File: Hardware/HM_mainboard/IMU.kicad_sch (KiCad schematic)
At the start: 12 parts, among them U5 BNO055, U6 MC6470

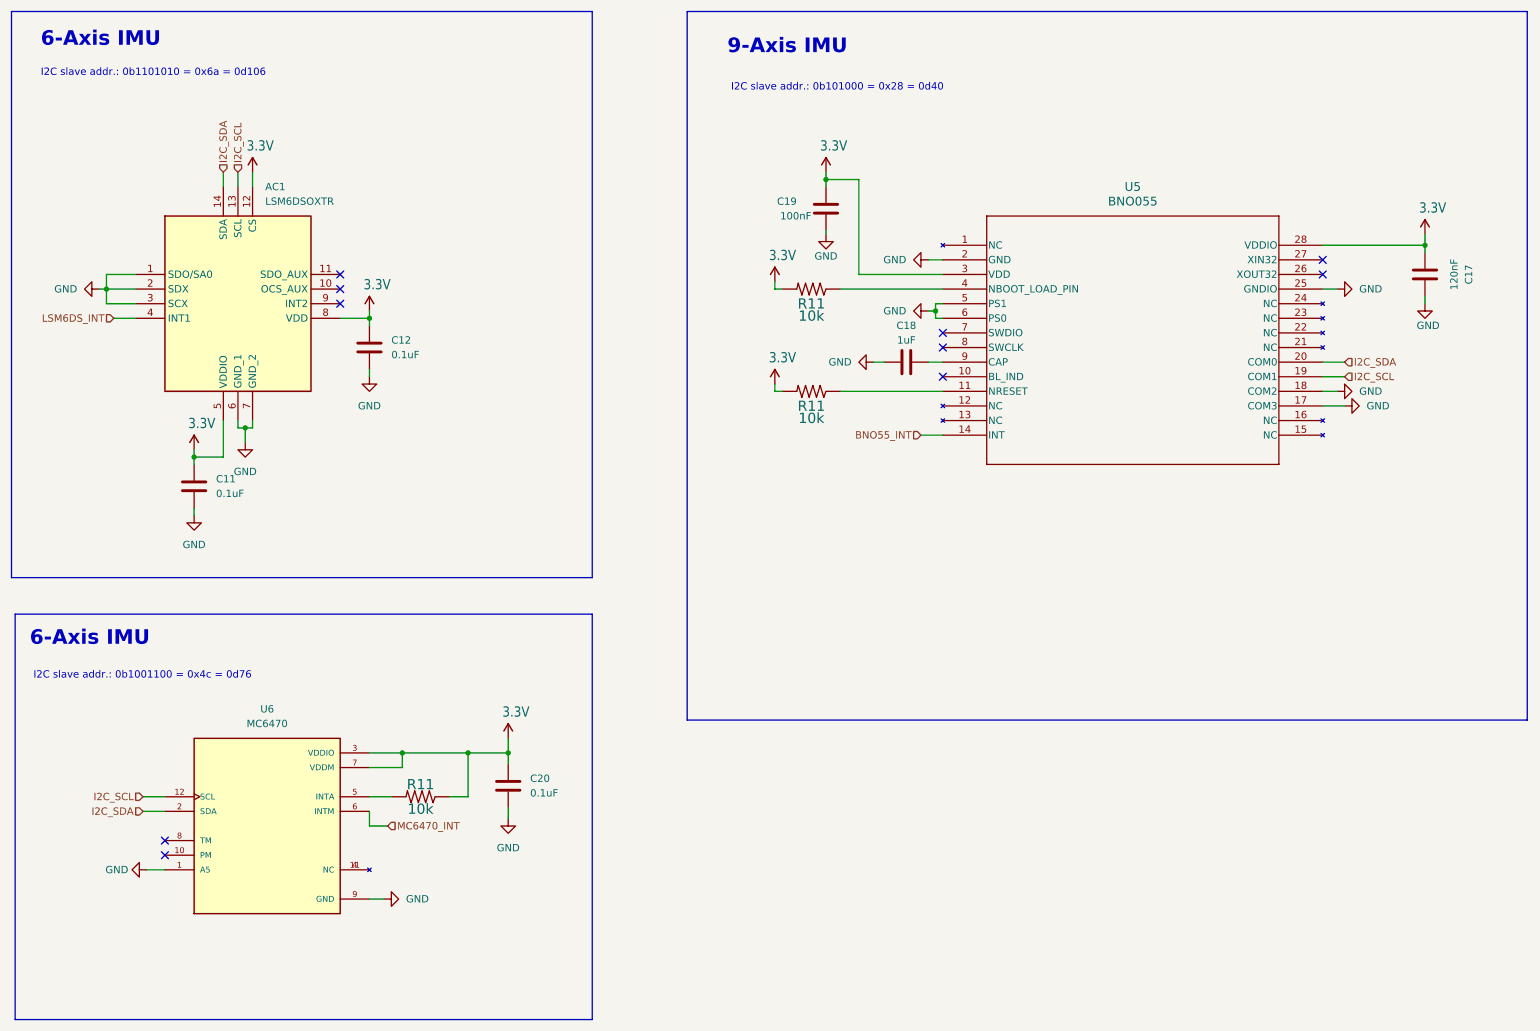
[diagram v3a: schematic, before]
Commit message: Added pull-ups to i2c connections
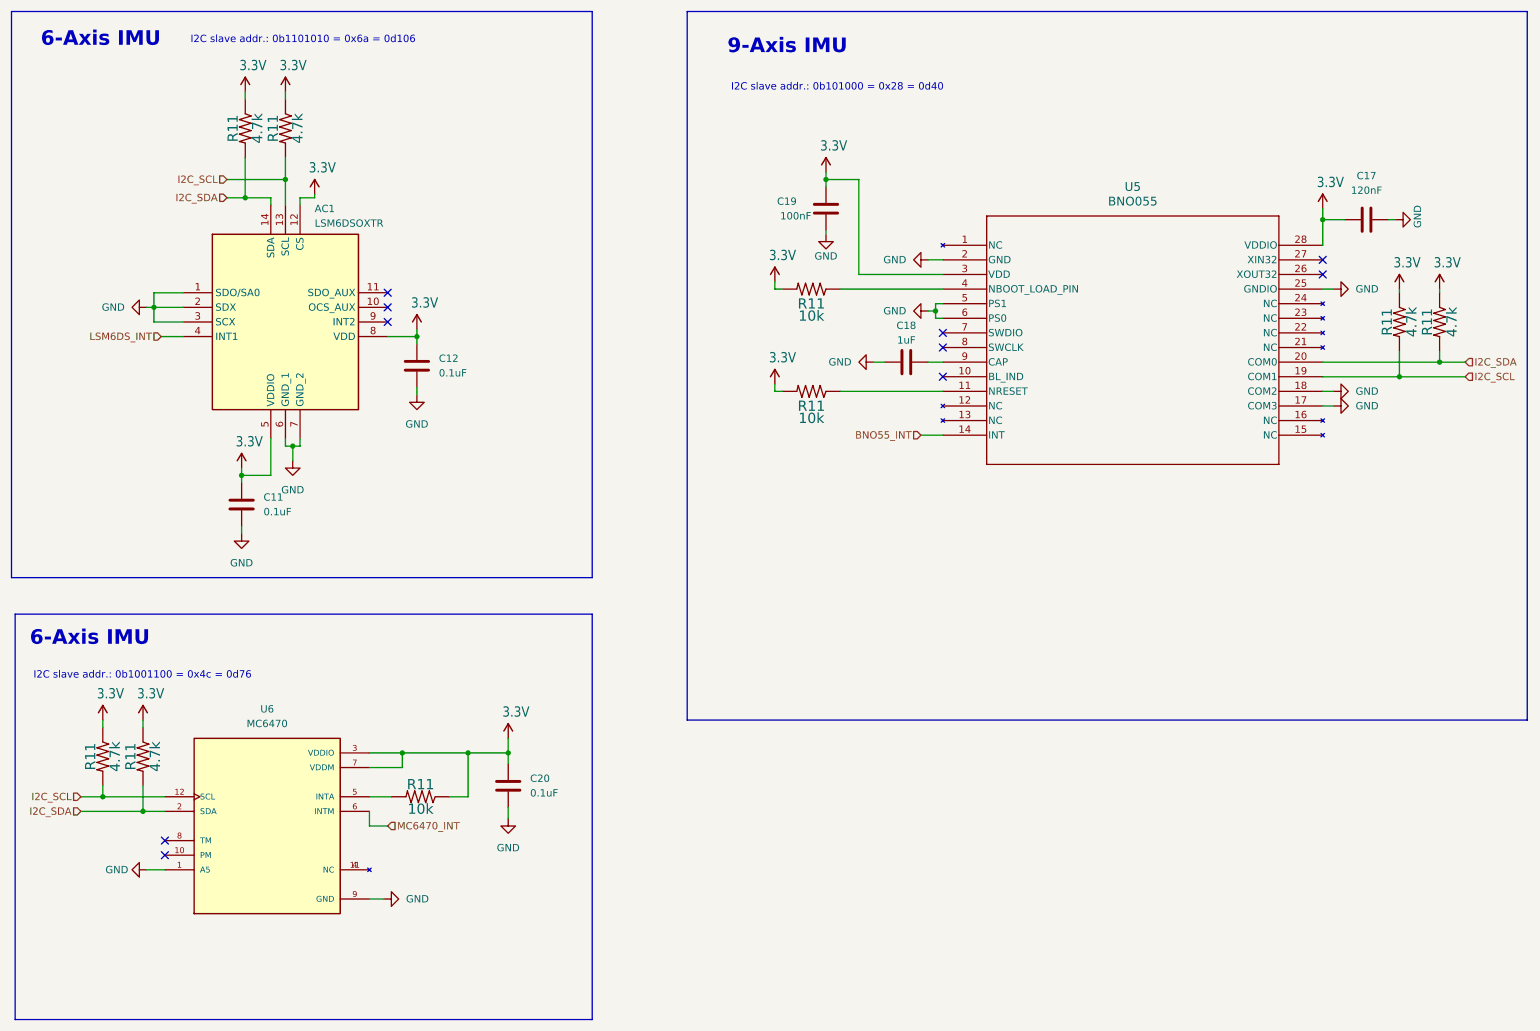
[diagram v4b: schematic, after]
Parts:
- added R11 (x6): 4.7k, Resistor_SMD:R_0603_1608Metric_Pad0.98x0.95mm_HandSolder, symbol esp32-thing-eagle-import:10KOHM-1/10W-1%(0603)0603
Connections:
- net 3.3V: now also R11.1, R11.1, R11.1, R11.1, R11.1, R11.1
- net I2C_SCL: now also R11.2, R11.2, R11.2
- net I2C_SDA: now also R11.2, R11.2, R11.2
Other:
- moved on the sheet: AC1, C11, C12, C17

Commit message: Started component placement for PCB
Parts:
- renumbered C11 to C15, C12 to C16, C20 to C17, C19 to C18, C18 to C19, C17 to C20, U6 to U5, U5 to U6

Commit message: Updated footprint of auxiliary jacks, routed first version of PCB
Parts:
- removed R11 (x6): 4.7k, Resistor_SMD:R_0603_1608Metric_Pad0.98x0.95mm_HandSolder, symbol esp32-thing-eagle-import:10KOHM-1/10W-1%(0603)0603

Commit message: Added BOM
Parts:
- AC1: Mouser (none) -> LSM6DSOXTR
- C15, C16, C17: value 0.1uF -> 100nF; Digikey (none) -> 1276-CL10B104KB8NNNLCT-ND; Mouser (none) -> 581-06035C104K4; RS Components (none) -> 200-6519
- C18: Digikey (none) -> 1276-CL10B104KB8NNNLCT-ND; Mouser (none) -> 581-06035C104K4; RS Components (none) -> 200-6519
- C19: value 1uF -> 1.0uF-25V-(+80/-20%); Mouser (none) -> F921E105KPA
- C20: value 120nF -> 100nF; Digikey (none) -> 1276-CL10B104KB8NNNLCT-ND; Mouser (none) -> 581-06035C104K4; RS Components (none) -> 200-6519
- U5: Mouser (none) -> MC6470; Mouser Price/Stock (none) -> https://www.mouser.at/ProductDetail/MEMSIC/MC6470?qs=u6%2FI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
- U6: Digikey (none) -> 828-1058; Mouser Price/Stock (none) -> https://www.digikey.at/en/products/detail/bosch-sensortec/B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
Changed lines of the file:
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@@
       (effects (font (size 1.27 1.27)))
     )
-    (property "Value" "1uF" (at 172.085 73.66 90)
+    (property "Value" "1.0uF-25V-(+80/-20%)" (at 172.085 73.66 90)
       (effects (font (size 1.27 1.27)))
     )
@@
     )
     (property "Datasheet" "~" (at 172.085 77.47 0)
+      (effects (font (size 1.27 1.27)) hide)
+    )
+    (property "Mouser" "F921E105KPA" (at 172.085 77.47 0)
+      (effects (font (size 1.27 1.27)) hide)
+    )
+    (property "Reichelt" "" (at 172.085 77.47 0)
       (effects (font (size 1.27 1.27)) hide)
     )
@@
       (effects (font (size 1.27 1.27)) hide)
     )
+    (property "Reichelt" "" (at 155.575 64.77 0)
+      (effects (font (size 1.27 1.27)) hide)
+    )
     (pin "1")
     (pin "2")
@@
       (effects (font (size 1.27 1.27)))
     )
-    (property "Value" "120nF" (at 252.095 47.625 90)
+    (property "Value" "100nF" (at 252.095 47.625 90)
       (effects (font (size 1.27 1.27)))
     )
@@
     )
     (property "Datasheet" "~" (at 252.095 52.705 0)
+      (effects (font (size 1.27 1.27)) hide)
+    )
+    (property "Reichelt" "" (at 252.095 52.705 0)
+      (effects (font (size 1.27 1.27)) hide)
+    )
+    (property "Digikey" "1276-CL10B104KB8NNNLCT-ND" (at 252.095 52.705 0)
+      (effects (font (size 1.27 1.27)) hide)
+    )
+    (property "Mouser" "581-06035C104K4" (at 252.095 52.705 0)
+      (effects (font (size 1.27 1.27)) hide)
+    )
+    (property "RS Components" "200-6519" (at 252.095 52.705 0)
       (effects (font (size 1.27 1.27)) hide)
     )
@@
       (effects (font (size 1.27 1.27)) (justify left))
     )
-    (property "Value" "0.1uF" (at 60.325 103.505 0)
+    (property "Value" "100nF" (at 60.325 103.505 0)
       (effects (font (size 1.27 1.27)) (justify left))
     )
@@
     )
     (property "Datasheet" "~" (at 56.515 102.235 0)
+      (effects (font (size 1.27 1.27)) hide)
+    )
+    (property "Reichelt" "" (at 56.515 102.235 0)
+      (effects (font (size 1.27 1.27)) hide)
+    )
+    (property "Digikey" "1276-CL10B104KB8NNNLCT-ND" (at 56.515 102.235 0)
+      (effects (font (size 1.27 1.27)) hide)
+    )
+    (property "Mouser" "581-06035C104K4" (at 56.515 102.235 0)
+      (effects (font (size 1.27 1.27)) hide)
+    )
+    (property "RS Components" "200-6519" (at 56.515 102.235 0)
       (effects (font (size 1.27 1.27)) hide)
     )
@@
       (effects (font (size 1.27 1.27)) (justify bottom) hide)
     )
-    (property "Datasheet" "" (at 60.96 158.115 0)
+    (property "Datasheet" "https://www.mouser.at/datasheet/2/821/MC6470_Datasheet_APS_048_0033v1_7_1-3003085.pdf" (at 60.96 158.115 0)
       (effects (font (size 1.27 1.27)) hide)
     )
     (property "MF" "Mcube Inc." (at 60.96 158.115 0)
       (effects (font (size 1.27 1.27)) (justify bottom) hide)
+    )
+    (property "Mouser" "MC6470" (at 60.96 158.115 0)
+      (effects (font (size 1.27 1.27)) hide)
+    )
+    (property "Mouser Price/Stock" "https://www.mouser.at/ProductDetail/MEMSIC/MC6470?qs=u6%2FIMcj1sDuOjN54xX4NKQ%3D%3D" (at 60.96 158.115 0)
+      (effects (font (size 1.27 1.27)) hide)
+    )
+    (property "Reichelt" "" (at 60.96 158.115 0)
+      (effects (font (size 1.27 1.27)) hide)
     )
     (pin "1")
@@
       (effects (font (size 1.27 1.27)) (justify left))
     )
-    (property "Value" "0.1uF" (at 90.805 79.375 0)
+    (property "Value" "100nF" (at 90.805 79.375 0)
       (effects (font (size 1.27 1.27)) (justify left))
     )
@@
     )
     (property "Datasheet" "~" (at 86.995 78.105 0)
+      (effects (font (size 1.27 1.27)) hide)
+    )
+    (property "Reichelt" "" (at 86.995 78.105 0)
+      (effects (font (size 1.27 1.27)) hide)
+    )
+    (property "Digikey" "1276-CL10B104KB8NNNLCT-ND" (at 86.995 78.105 0)
+      (effects (font (size 1.27 1.27)) hide)
+    )
+    (property "Mouser" "581-06035C104K4" (at 86.995 78.105 0)
+      (effects (font (size 1.27 1.27)) hide)
+    )
+    (property "RS Components" "200-6519" (at 86.995 78.105 0)
       (effects (font (size 1.27 1.27)) hide)
     )
@@
       (effects (font (size 1.27 1.27)) (justify left))
     )
-    (property "Value" "0.1uF" (at 106.68 152.4 0)
+    (property "Value" "100nF" (at 106.68 152.4 0)
       (effects (font (size 1.27 1.27)) (justify left))
     )
@@
     )
     (property "Datasheet" "~" (at 102.87 151.13 0)
+      (effects (font (size 1.27 1.27)) hide)
+    )
+    (property "Reichelt" "" (at 102.87 151.13 0)
+      (effects (font (size 1.27 1.27)) hide)
+    )
+    (property "Digikey" "1276-CL10B104KB8NNNLCT-ND" (at 102.87 151.13 0)
+      (effects (font (size 1.27 1.27)) hide)
+    )
+    (property "Mouser" "581-06035C104K4" (at 102.87 151.13 0)
+      (effects (font (size 1.27 1.27)) hide)
+    )
+    (property "RS Components" "200-6519" (at 102.87 151.13 0)
       (effects (font (size 1.27 1.27)) hide)
     )
@@
     (property "Datasheet" "https://www.bosch-sensortec.com/media/boschsensortec/downloads/datasheets/bst-bno055-ds000.pdf" (at 178.435 57.15 0)
       (effects (font (size 1.27 1.27) italic) hide)
+    )
+    (property "Digikey" "828-1058" (at 178.435 57.15 0)
+      (effects (font (size 1.27 1.27)) hide)
+    )
+    (property "Mouser Price/Stock" "https://www.digikey.at/en/products/detail/bosch-sensortec/BNO055/6136301" (at 178.435 57.15 0)
+      (effects (font (size 1.27 1.27)) hide)
+    )
+    (property "Reichelt" "" (at 178.435 57.15 0)
+      (effects (font (size 1.27 1.27)) hide)
     )
     (pin "1")
@@
       (effects (font (size 1.27 1.27)) hide)
     )
+    (property "Reichelt" "" (at 87.63 153.035 0)
+      (effects (font (size 1.27 1.27)) hide)
+    )
     (pin "1")
     (pin "2")
@@
       (effects (font (size 1.27 1.27)) hide)
     )
+    (property "Reichelt" "" (at 158.115 50.8 0)
+      (effects (font (size 1.27 1.27)) hide)
+    )
+    (property "Digikey" "1276-CL10B104KB8NNNLCT-ND" (at 158.115 50.8 0)
+      (effects (font (size 1.27 1.27)) hide)
+    )
+    (property "Mouser" "581-06035C104K4" (at 158.115 50.8 0)
+      (effects (font (size 1.27 1.27)) hide)
+    )
+    (property "RS Components" "200-6519" (at 158.115 50.8 0)
+      (effects (font (size 1.27 1.27)) hide)
+    )
     (pin "1")
     (pin "2")
@@
     (property "Manufacturer_Part_Number" "LSM6DSOXTR" (at 78.105 852.705 0)
       (effects (font (size 1.27 1.27)) (justify left top) hide)
+    )
+    (property "Mouser" "LSM6DSOXTR" (at 46.355 65.405 0)
+      (effects (font (size 1.27 1.27)) hide)
+    )
+    (property "Reichelt" "" (at 46.355 65.405 0)
+      (effects (font (size 1.27 1.27)) hide)
     )
     (pin "1")
@@
       (effects (font (size 1.27 1.27)) hide)
     )
+    (property "Reichelt" "" (at 155.575 82.55 0)
+      (effects (font (size 1.27 1.27)) hide)
+    )

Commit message: Updated BOM
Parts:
- C15, C16, C17, C18, C20: Digikey 1276-CL10B104KB8NNNLCT-ND -> 1276-CL10B104KB8NNNLCT
- C19: Mouser F921E105KPA -> 647-F921E105KPA
- R11: value 10k -> 10k/1%; Mouser (none) -> 660-RN73H1JT1002F100
- U5: Mouser MC6470 -> 498-MC6470
- U6: Mouser (none) -> 262-BNO055
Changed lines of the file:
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@@
       (effects (font (size 1.27 1.27)) hide)
     )
-    (property "Mouser" "F921E105KPA" (at 172.085 77.47 0)
+    (property "Mouser" "647-F921E105KPA" (at 172.085 77.47 0)
       (effects (font (size 1.27 1.27)) hide)
     )
@@
       (effects (font (size 1.778 1.778)) (justify bottom))
     )
-    (property "Value" "10k" (at 155.575 70.485 0)
+    (property "Value" "10k/1%" (at 155.575 70.485 0)
       (effects (font (size 1.778 1.778)) (justify top))
     )
@@
     )
     (property "Reichelt" "" (at 155.575 64.77 0)
+      (effects (font (size 1.27 1.27)) hide)
+    )
+    (property "Mouser" "660-RN73H1JT1002F100" (at 155.575 64.77 0)
       (effects (font (size 1.27 1.27)) hide)
     )
@@
       (effects (font (size 1.27 1.27)) hide)
     )
-    (property "Digikey" "1276-CL10B104KB8NNNLCT-ND" (at 252.095 52.705 0)
+    (property "Digikey" "1276-CL10B104KB8NNNLCT" (at 252.095 52.705 0)
       (effects (font (size 1.27 1.27)) hide)
     )
@@
       (effects (font (size 1.27 1.27)) hide)
     )
-    (property "Digikey" "1276-CL10B104KB8NNNLCT-ND" (at 56.515 102.235 0)
+    (property "Digikey" "1276-CL10B104KB8NNNLCT" (at 56.515 102.235 0)
       (effects (font (size 1.27 1.27)) hide)
     )
@@
       (effects (font (size 1.27 1.27)) (justify bottom) hide)
     )
-    (property "Mouser" "MC6470" (at 60.96 158.115 0)
+    (property "Mouser" "498-MC6470" (at 60.96 158.115 0)
       (effects (font (size 1.27 1.27)) hide)
     )
@@
       (effects (font (size 1.27 1.27)) hide)
     )
-    (property "Digikey" "1276-CL10B104KB8NNNLCT-ND" (at 86.995 78.105 0)
+    (property "Digikey" "1276-CL10B104KB8NNNLCT" (at 86.995 78.105 0)
       (effects (font (size 1.27 1.27)) hide)
     )
@@
       (effects (font (size 1.27 1.27)) hide)
     )
-    (property "Digikey" "1276-CL10B104KB8NNNLCT-ND" (at 102.87 151.13 0)
+    (property "Digikey" "1276-CL10B104KB8NNNLCT" (at 102.87 151.13 0)
       (effects (font (size 1.27 1.27)) hide)
     )
@@
     )
     (property "Reichelt" "" (at 178.435 57.15 0)
+      (effects (font (size 1.27 1.27)) hide)
+    )
+    (property "Mouser" "262-BNO055" (at 178.435 57.15 0)
       (effects (font (size 1.27 1.27)) hide)
     )
@@
       (effects (font (size 1.778 1.778)) (justify bottom))
     )
-    (property "Value" "10k" (at 87.63 156.21 0)
+    (property "Value" "10k/1%" (at 87.63 156.21 0)
       (effects (font (size 1.778 1.778)) (justify top))
     )
@@
     )
     (property "Reichelt" "" (at 87.63 153.035 0)
+      (effects (font (size 1.27 1.27)) hide)
+    )
+    (property "Mouser" "660-RN73H1JT1002F100" (at 87.63 153.035 0)
       (effects (font (size 1.27 1.27)) hide)
     )
@@
       (effects (font (size 1.27 1.27)) hide)
     )
-    (property "Digikey" "1276-CL10B104KB8NNNLCT-ND" (at 158.115 50.8 0)
+    (property "Digikey" "1276-CL10B104KB8NNNLCT" (at 158.115 50.8 0)
       (effects (font (size 1.27 1.27)) hide)
     )
@@
       (effects (font (size 1.778 1.778)) (justify bottom))
     )
-    (property "Value" "10k" (at 155.575 88.265 0)
+    (property "Value" "10k/1%" (at 155.575 88.265 0)
       (effects (font (size 1.778 1.778)) (justify top))
     )
@@
       (effects (font (size 1.27 1.27)) hide)
     )
+    (property "Mouser" "660-RN73H1JT1002F100" (at 155.575 82.55 0)
+      (effects (font (size 1.27 1.27)) hide)
+    )
